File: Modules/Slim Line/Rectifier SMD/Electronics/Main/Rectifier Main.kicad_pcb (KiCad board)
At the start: 2 copper layers, 38.1 x 101.6 mm, 34 parts, among them J1 Negative HW, J2 Full Wave, J3 In, J4 Positive HW, J5 Power, U1 TL074, U2 TL072

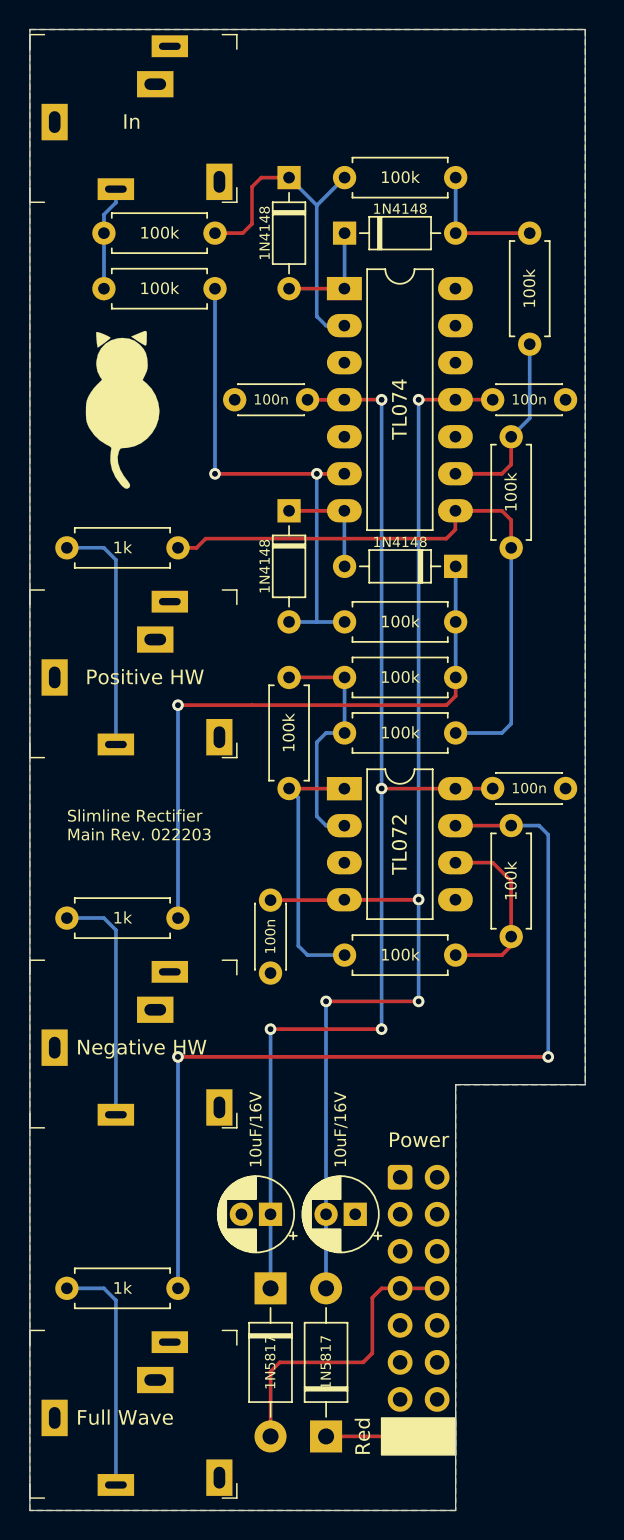
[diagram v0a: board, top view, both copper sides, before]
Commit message: Update Sync LFO
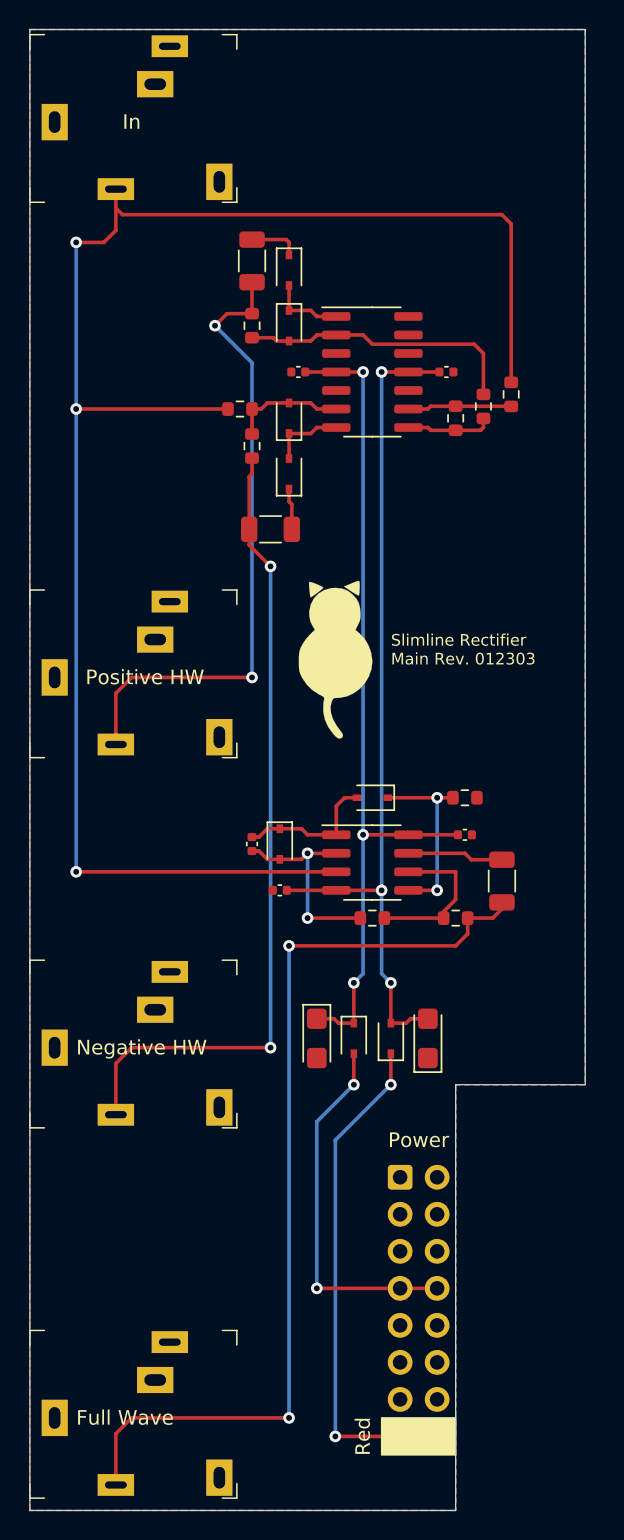
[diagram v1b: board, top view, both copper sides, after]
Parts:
- removed the R5 at (29.2, 44.5)
- removed the R6 at (17.8, 44.5)
- removed the R7 at (29.2, 48.3)
- removed the R8 at (21.6, 63.5)
- removed the R9 at (10.2, 86.4)
- removed the U2 at (21.6, 52.1)
- added C1: 22p, Capacitor_SMD:C_0402_1005Metric, F.Cu at (15.2, 55.9)
- added D1: 1N4148WS, Diode_SMD:D_SOD-323, F.Cu at (17.1, 55.9)
- added D2: 1N4148WS, Diode_SMD:D_SOD-323, F.Cu at (23.5, 52.7)
- added R1: 100k, Resistor_SMD:R_0603_1608Metric, F.Cu at (23.5, 61.0)
- added R2: 100k, Resistor_SMD:R_0603_1608Metric, F.Cu at (29.2, 61.0)
- added R3: 1k, Resistor_SMD:R_1206_3216Metric, F.Cu at (32.4, 58.4)
- added U1: TL082CDT, Package_SO:SOIC-8_3.9x4.9mm_P1.27mm, F.Cu at (23.5, 57.1)
- C2: renamed from C1; footprint Capacitor_THT:CP_Radial_D5.0mm_P2.00mm -> Capacitor_Tantalum_SMD:CP_EIA-3216-18_Kemet-A
- C3: renamed from C2; footprint Capacitor_THT:C_Disc_D4.3mm_W1.9mm_P5.00mm -> Capacitor_SMD:C_0402_1005Metric
- C4: renamed from C6; footprint Capacitor_THT:C_Disc_D4.3mm_W1.9mm_P5.00mm -> Capacitor_SMD:C_0402_1005Metric
- C5: renamed from C4; footprint Capacitor_THT:CP_Radial_D5.0mm_P2.00mm -> Capacitor_Tantalum_SMD:CP_EIA-3216-18_Kemet-A
- C6: renamed from C5; footprint Capacitor_THT:C_Disc_D4.3mm_W1.9mm_P5.00mm -> Capacitor_SMD:C_0402_1005Metric
- C7: renamed from C3; footprint Capacitor_THT:C_Disc_D4.3mm_W1.9mm_P5.00mm -> Capacitor_SMD:C_0402_1005Metric
- D3: renamed from D1; value 1N4148 -> 1N4148WS; footprint Diode_THT:D_DO-35_SOD27_P7.62mm_Horizontal -> Diode_SMD:D_SOD-323
- D4: renamed from D2; value 1N4148 -> 1N4148WS; footprint Diode_THT:D_DO-35_SOD27_P7.62mm_Horizontal -> Diode_SMD:D_SOD-323
- D5: renamed from D3; value 1N4148 -> 1N4148WS; footprint Diode_THT:D_DO-35_SOD27_P7.62mm_Horizontal -> Diode_SMD:D_SOD-323
- D6: renamed from D4; value 1N4148 -> 1N4148WS; footprint Diode_THT:D_DO-35_SOD27_P7.62mm_Horizontal -> Diode_SMD:D_SOD-323
- D7: renamed from D5; value 1N5817 -> 1N5819WS; footprint Diode_THT:D_DO-41_SOD81_P10.16mm_Horizontal -> Diode_SMD:D_SOD-323
- D8: renamed from D6; value 1N5817 -> 1N5819WS; footprint Diode_THT:D_DO-41_SOD81_P10.16mm_Horizontal -> Diode_SMD:D_SOD-323
- R10: renamed from R13; footprint Resistor_THT:R_Axial_DIN0207_L6.3mm_D2.5mm_P7.62mm_Horizontal -> Resistor_SMD:R_0603_1608Metric
- R11: renamed from R12; footprint Resistor_THT:R_Axial_DIN0207_L6.3mm_D2.5mm_P7.62mm_Horizontal -> Resistor_SMD:R_0603_1608Metric
- R12: renamed from R14; footprint Resistor_THT:R_Axial_DIN0207_L6.3mm_D2.5mm_P7.62mm_Horizontal -> Resistor_SMD:R_1206_3216Metric
- R4: footprint Resistor_THT:R_Axial_DIN0207_L6.3mm_D2.5mm_P7.62mm_Horizontal -> Resistor_SMD:R_0603_1608Metric
- R5: renamed from R1; footprint Resistor_THT:R_Axial_DIN0207_L6.3mm_D2.5mm_P7.62mm_Horizontal -> Resistor_SMD:R_0603_1608Metric
- R6: renamed from R3; footprint Resistor_THT:R_Axial_DIN0207_L6.3mm_D2.5mm_P7.62mm_Horizontal -> Resistor_SMD:R_0603_1608Metric
- R7: renamed from R2; footprint Resistor_THT:R_Axial_DIN0207_L6.3mm_D2.5mm_P7.62mm_Horizontal -> Resistor_SMD:R_1206_3216Metric
- R8: renamed from R10; footprint Resistor_THT:R_Axial_DIN0207_L6.3mm_D2.5mm_P7.62mm_Horizontal -> Resistor_SMD:R_0603_1608Metric
- R9: renamed from R11; footprint Resistor_THT:R_Axial_DIN0207_L6.3mm_D2.5mm_P7.62mm_Horizontal -> Resistor_SMD:R_0603_1608Metric
- U2: renamed from U1; value TL074 -> TL084CDT; footprint Package_DIP:DIP-14_W7.62mm_LongPads -> Package_SO:SOIC-14_3.9x8.7mm_P1.27mm
- moved C6 38.9 mm to (17.1, 59.1), turned to 0 degrees
- moved C7 38.2 mm to (28.6, 23.5), turned to 0 degrees
- moved C4 34.0 mm to (18.4, 23.5), turned to 0 degrees
- moved C3 31.7 mm to (29.8, 55.2), turned to 0 degrees
- moved R11 28.6 mm to (31.1, 25.9), turned to 90 degrees
- moved D8 27.7 mm to (24.8, 69.2)
- moved R7 27.4 mm to (16.5, 34.3)
- moved G*** 22.5 mm to (21.0, 43.2)
- moved R12 20.3 mm to (15.2, 15.9), turned to -90 degrees
- moved D7 18.1 mm to (22.2, 69.2)
- moved R5 13.6 mm to (15.2, 28.6), turned to -90 degrees
- moved D4 13.1 mm to (17.8, 30.5), turned to 90 degrees
- moved C5 13.1 mm to (27.3, 69.2), turned to 90 degrees
- moved C2 12.5 mm to (19.7, 69.2), turned to -90 degrees
- moved R6 12.5 mm to (14.4, 26.0)
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- renumbered J2 to J1, J1 to J2
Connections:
- D4 pad 1: Net-(D2-Pad1) (its old number) -> Net-(D4-Pad1)
- D5 pad 1: Net-(D3-Pad1) (its old number) -> Net-(D5-Pad1)
- D5 pad 2: Net-(D3-Pad2) (its old number) -> Net-(D5-Pad2)
- D6 pad 1: Net-(D3-Pad2) (its old number) -> Net-(D6-Pad1)
- D6 pad 2: Net-(D4-Pad2) -> Net-(D5-Pad1)
- J2 pad T: Net-(J1-PadT) (its old number) -> Net-(J2-PadT)
- R10 pad 1: Net-(D4-Pad2) -> Net-(J3-PadT)
- R11 pad 1: Net-(J3-PadT) -> Net-(R9-Pad2)
- R11 pad 2: Net-(D3-Pad1) (its old number) -> Net-(D5-Pad2)
- R12 pad 1: Net-(R11-Pad2) -> Net-(D6-Pad1)
- R4 pad 1: Net-(R4-Pad1) -> GND
- R5 pad 2: Net-(D2-Pad1) (its old number) -> Net-(J2-PadT)
- R7 pad 1: Net-(D2-Pad1) (its old number) -> Net-(D4-Pad1)
- R7 pad 2: Net-(J1-PadT) (its old number) -> Net-(J2-PadT)
- R8 pad 1: Net-(D3-Pad1) (its old number) -> Net-(D5-Pad2)
- R8 pad 2: Net-(D4-Pad2) -> Net-(J4-PadT)
- R9 pad 2: Net-(R11-Pad2) -> Net-(R9-Pad2)
- U2 pad 1: Net-(D3-Pad2) (its old number) -> Net-(D5-Pad1)
- U2 pad 2: Net-(D3-Pad1) (its old number) -> Net-(D5-Pad2)
- U2 pad 8: Net-(R11-Pad2) -> Net-(R9-Pad2)
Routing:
- net Net-(J3-PadT): track 7.17 -> 115.8 mm, vias 0 -> 3
- net Net-(J2-PadT): track 0.00 -> 55.7 mm, vias 0 -> 2
- net Net-(D2-Pad1): track 63.1 -> 12.8 mm
- net Net-(J1-PadT): track 16.4 -> 65.0 mm, vias 0 -> 2
- net Net-(R11-Pad2): track 43.0 -> 0.00 mm
- net Net-(D2-Pad1) (its old number): track 42.8 -> 0.00 mm, vias 1 -> 0
- net Net-(D3-Pad2): track 35.5 -> 7.84 mm, vias 2 -> 0
- net Net-(D8-Pad1): track 7.62 -> 34.8 mm, vias 0 -> 2
- net Net-(J4-PadT): track 16.4 -> 43.5 mm, vias 0 -> 2
- net -12V: track 82.6 -> 58.1 mm, vias 4 -> 3
- net Net-(D3-Pad1) (its old number): track 23.3 -> 0.00 mm
- net +12V: track 81.3 -> 58.1 mm, vias 4 -> 3
- net Net-(D5-Pad2): track 0.00 -> 19.5 mm
- net Net-(R6-Pad2): track 18.3 -> 0.00 mm
- net Net-(R5-Pad2): track 17.0 -> 0.00 mm
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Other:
- board text added: "JLCJLCJLCJLC"
- board text added: "Slimline Rectifier Main Rev. 012303"
- board text removed: "Slimline Rectifier Main Rev. 022203"
